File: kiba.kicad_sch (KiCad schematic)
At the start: 15 parts, among them J1 Raspberry_Pi_2_3, J2 Conn_01x02, Q1 2N7002NXAKR, U1 LM1117MP-3.3

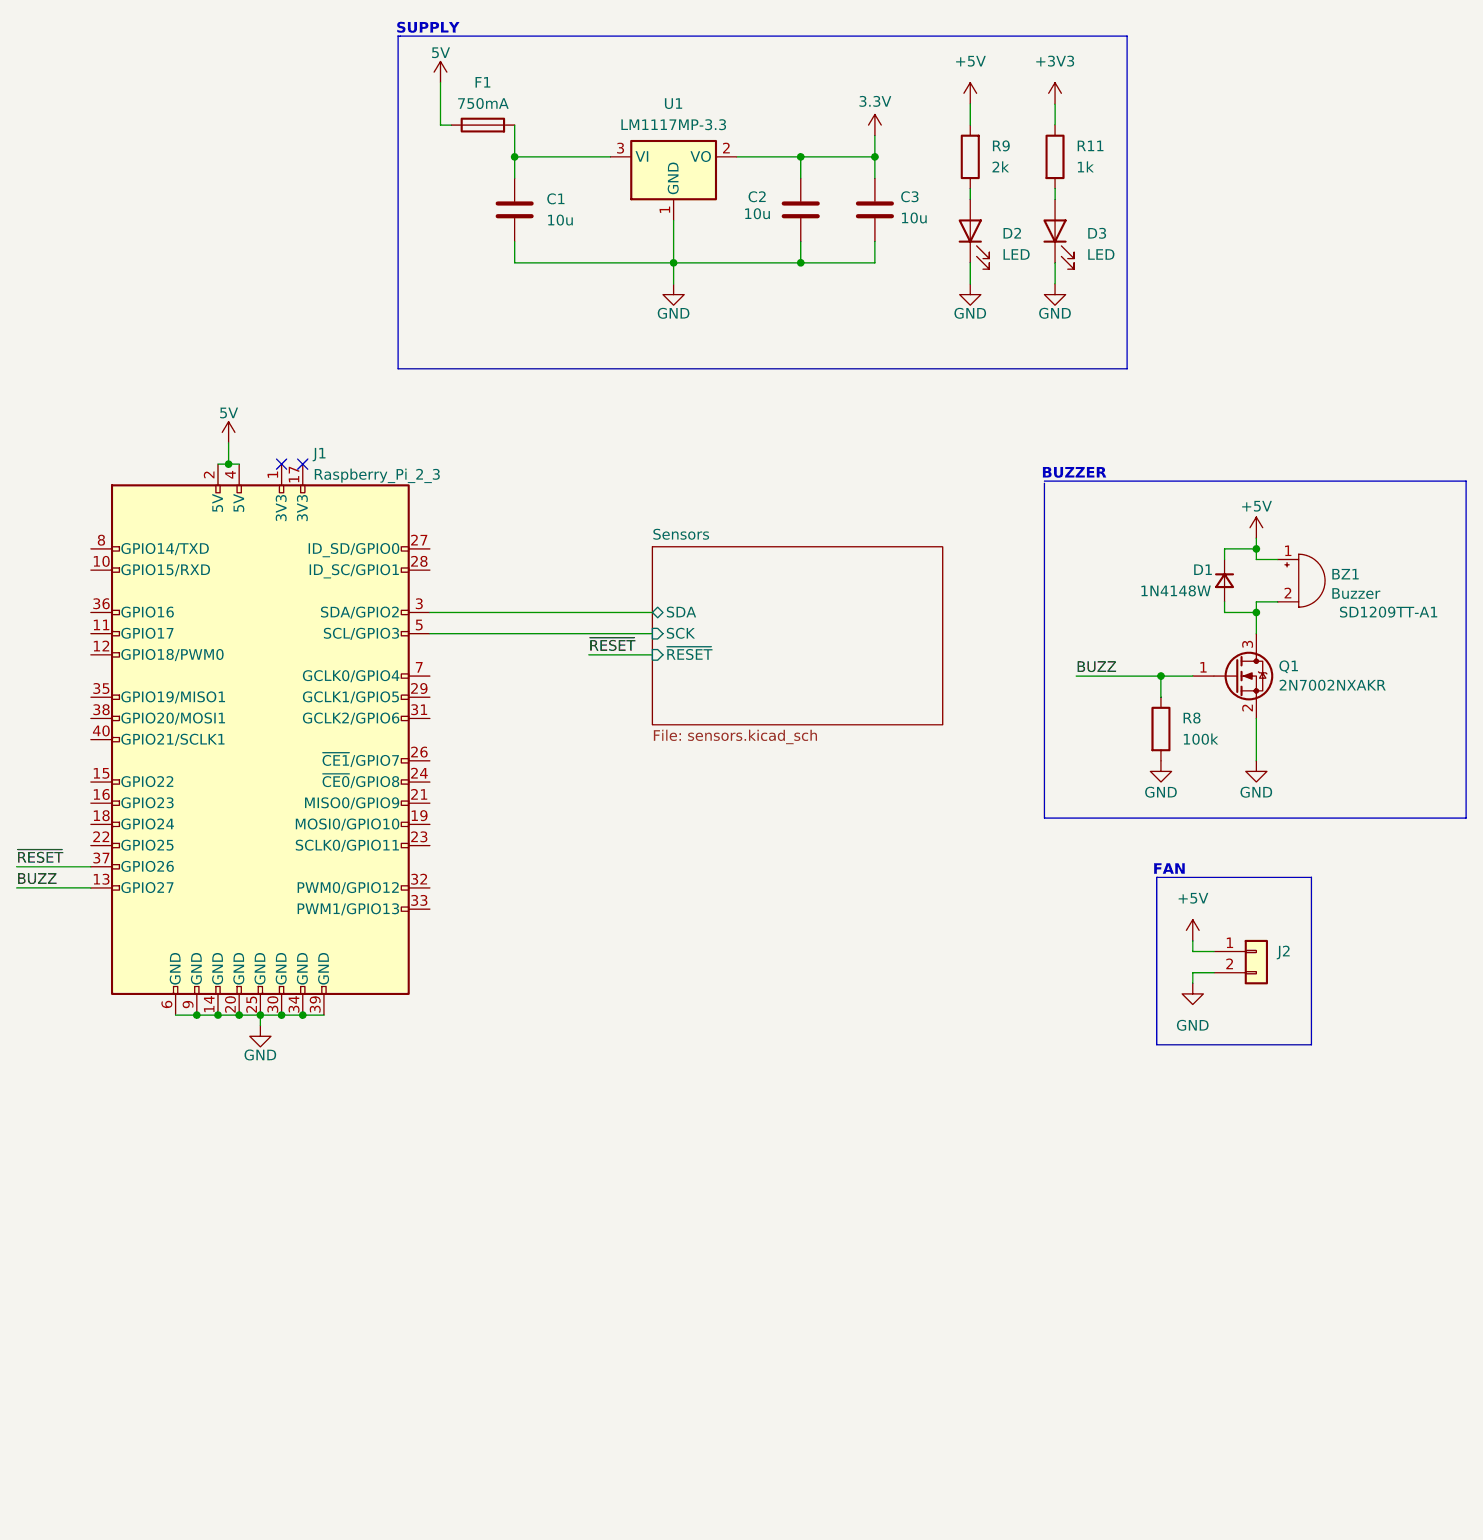
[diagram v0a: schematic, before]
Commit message: fix: fllags and footprints
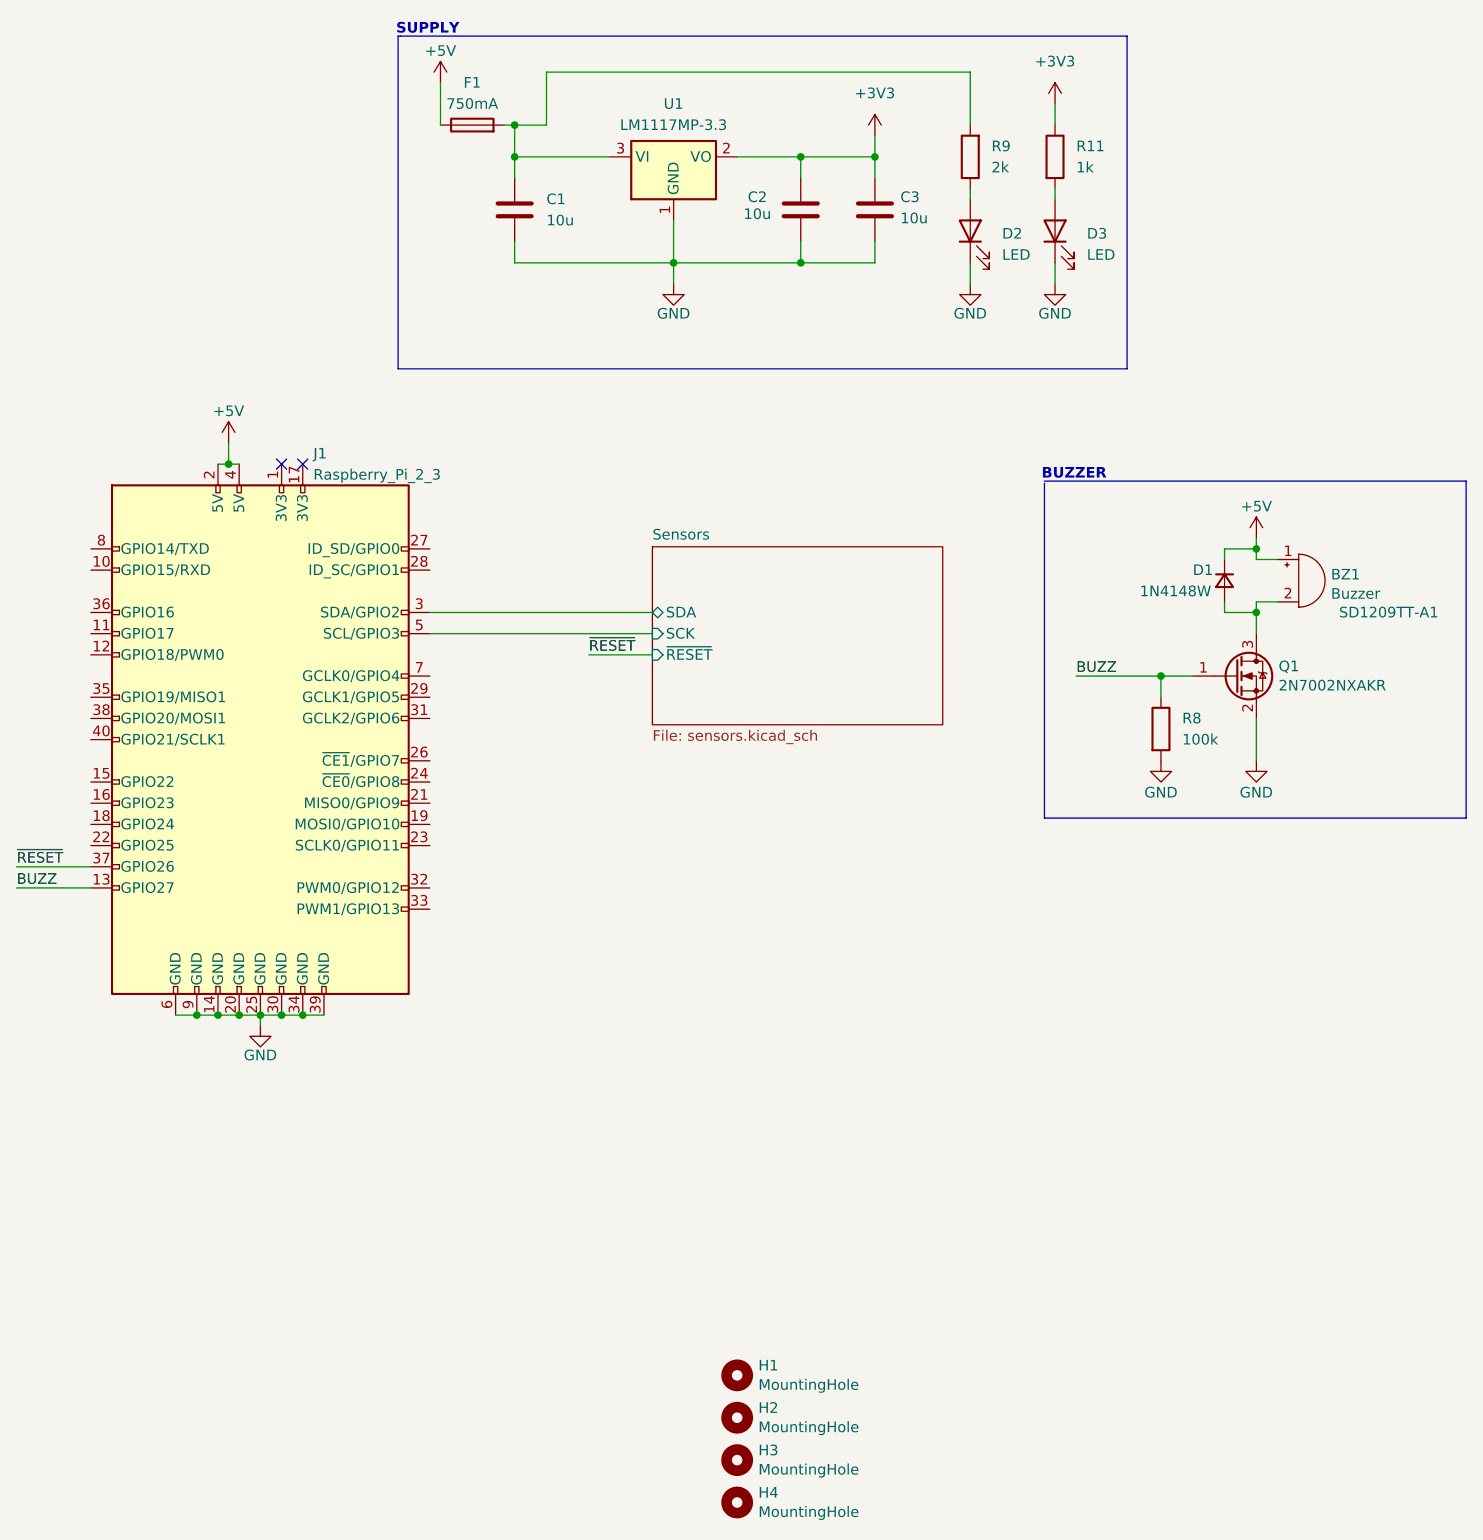
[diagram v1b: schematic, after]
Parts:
- removed J2: Conn_01x02, Connector_PinHeader_2.54mm:PinHeader_1x02_P2.54mm_Vertical, symbol Connector_Generic:Conn_01x02
- added H1, H2, H3, H4: MountingHole, Local:MountingHole_3.2mm_M3_ISO14580, symbol Mechanical:MountingHole
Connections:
- net 3.3V is gone; now on net +3V3: C2.1, C3.1, U1.2 (VO)
- net 5V is gone; now on net +5V: F1.1, J1.2 (5V), J1.4 (5V)
- net +5V: no longer R9.2
- net at C1.1, F1.2, U1.3 (VI): now also R9.2
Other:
- note removed: "FAN"
- moved on the sheet: F1

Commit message: fix: drc errors
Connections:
- no-connect marks 2 -> 26
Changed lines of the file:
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@@
+	)
+	(no_connect
+		(at 115.57 113.03)
+	)
+	(no_connect
+		(at 74.93 92.71)
+	)
+	(no_connect
+		(at 74.93 100.33)
+	)
+	(no_connect
+		(at 74.93 82.55)
+	)
+	(no_connect
+		(at 115.57 120.65)
+	)
+	(no_connect
+		(at 115.57 100.33)
+	)
+	(no_connect
+		(at 74.93 107.95)
+	)
+	(no_connect
+		(at 115.57 80.01)
+	)
+	(no_connect
+		(at 74.93 87.63)
+	)
+	(no_connect
+		(at 74.93 97.79)
+	)
+	(no_connect
+		(at 115.57 110.49)
+	)
+	(no_connect
+		(at 115.57 123.19)
+	)
+	(no_connect
+		(at 74.93 90.17)
+	)
+	(no_connect
+		(at 74.93 115.57)
+	)
+	(no_connect
+		(at 115.57 115.57)
+	)
+	(no_connect
+		(at 74.93 113.03)
+	)
+	(no_connect
+		(at 74.93 80.01)
+	)
+	(no_connect
+		(at 115.57 107.95)
+	)
+	(no_connect
+		(at 115.57 97.79)
+	)
+	(no_connect
+		(at 115.57 105.41)
+	)
+	(no_connect
+		(at 115.57 95.25)
+	)
+	(no_connect
+		(at 74.93 102.87)
+	)
+	(no_connect
+		(at 115.57 82.55)
 	)
 	(no_connect
 		(at 100.33 69.85)
 	)
+	(no_connect
+		(at 74.93 110.49)
+	)
 	(wire

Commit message: prod: add MPN
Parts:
- BZ1: MPN (none) -> SD1209TT-A1; PN SD1209TT-A1 -> (none)
- D1: MPN (none) -> 1N4148W
- D2, D3: MPN (none) -> TLMS1000-GS15
- J1: MPN (none) -> 2.54-2*20
- Q1: MPN (none) -> 2N7002NXAKR
- U1: MPN (none) -> LM1117MP-3.3/TR
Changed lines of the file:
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@@
 			)
 		)
-		(property "PN" "SD1209TT-A1"
+		(property "MPN" "SD1209TT-A1"
 			(at 230.505 87.63 0)
 			(effects
@@
 			)
 		)
+		(property "MPN" " TLMS1000-GS15 "
+			(at 190.5 41.91 90)
+			(effects
+				(font
+					(size 1.27 1.27)
+				)
+				(hide yes)
+			)
+		)
 		(pin "1"
 		)
@@
 			)
 		)
+		(property "MPN" "LM1117MP-3.3/TR"
+			(at 144.78 33.02 0)
+			(effects
+				(font
+					(size 1.27 1.27)
+				)
+				(hide yes)
+			)
+		)
 		(pin "1"
 		)
@@
 			)
 		)
+		(property "MPN" "1N4148W"
+			(at 210.82 83.82 90)
+			(effects
+				(font
+					(size 1.27 1.27)
+				)
+				(hide yes)
+			)
+		)
 		(pin "1"
 		)
@@
 			)
 		)
+		(property "MPN" "2.54-2*20"
+			(at 95.25 102.87 0)
+			(effects
+				(font
+					(size 1.27 1.27)
+				)
+				(hide yes)
+			)
+		)
 		(pin "1"
 		)
@@
 			)
 		)
+		(property "MPN" " TLMS1000-GS15 "
+			(at 180.34 41.91 90)
+			(effects
+				(font
+					(size 1.27 1.27)
+				)
+				(hide yes)
+			)
+		)
 		(pin "1"
 		)
@@
 			(at 212.09 95.25 0)
 			(effects
+				(font
+					(size 1.27 1.27)
+				)
+				(hide yes)
+			)
+		)
+		(property "MPN" "2N7002NXAKR"
+			(at 212.09 95.25 0)
+			(effects

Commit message: Added JLCPCB part numbers and generated BOM
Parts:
- BZ1: LCSC (none) -> C91083
- D1: LCSC (none) -> C2099
- D2: LCSC (none) -> C2288
- D3: LCSC (none) -> C12624
- F1: LCSC (none) -> C206991
- J1: LCSC (none) -> C2977589
- Q1: LCSC (none) -> C551416
- U1: LCSC (none) -> C498153
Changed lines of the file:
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@@
+			)
+		)
+		(property "LCSC" "C91083"
+			(at 223.5708 83.0834 0)
+			(effects
+				(font
+					(size 1.27 1.27)
+				)
+				(hide yes)
 			)
 		)
@@
 			)
 		)
+		(property "LCSC" "C12624"
+			(at 194.31 42.2274 0)
+			(effects
+				(font
+					(size 1.27 1.27)
+				)
+				(hide yes)
+			)
+		)
 		(pin "1"
 		)
@@
 		(property "Description" "Fuse"
 			(at 120.65 29.21 0)
+			(effects
+				(font
+					(size 1.27 1.27)
+				)
+				(hide yes)
+			)
+		)
+		(property "LCSC" "C206991"
+			(at 120.65 24.13 0)
 			(effects
 				(font
@@
 			)
 		)
+		(property "LCSC" "C498153"
+			(at 144.78 26.67 0)
+			(effects
+				(font
+					(size 1.27 1.27)
+				)
+				(hide yes)
+			)
+		)
 		(pin "1"
 		)
@@
 			)
 		)
+		(property "LCSC" "C2099"
+			(at 207.01 82.55 0)
+			(effects
+				(font
+					(size 1.27 1.27)
+				)
+				(hide yes)
+			)
+		)
 		(pin "1"
 		)
@@
 			)
 		)
+		(property "LCSC" "C2977589"
+			(at 101.6 68.58 0)
+			(effects
+				(font
+					(size 1.27 1.27)
+				)
+				(hide yes)
+			)
+		)
 		(pin "1"
 		)
@@
 			)
 		)
+		(property "LCSC" "C2288"
+			(at 184.15 42.2274 0)
+			(effects
+				(font
+					(size 1.27 1.27)
+				)
+				(hide yes)
+			)
+		)
 		(pin "1"
 		)
@@
 			(effects
 				(font
+					(size 1.27 1.27)
+				)
+				(hide yes)
+			)
+		)
+		(property "LCSC" "C551416"
+			(at 217.297 94.0816 0)
+			(effects
+				(font
